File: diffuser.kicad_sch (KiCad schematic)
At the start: 4 parts, among them J5 691137710002, U8 BSR802NL6327HTSA1

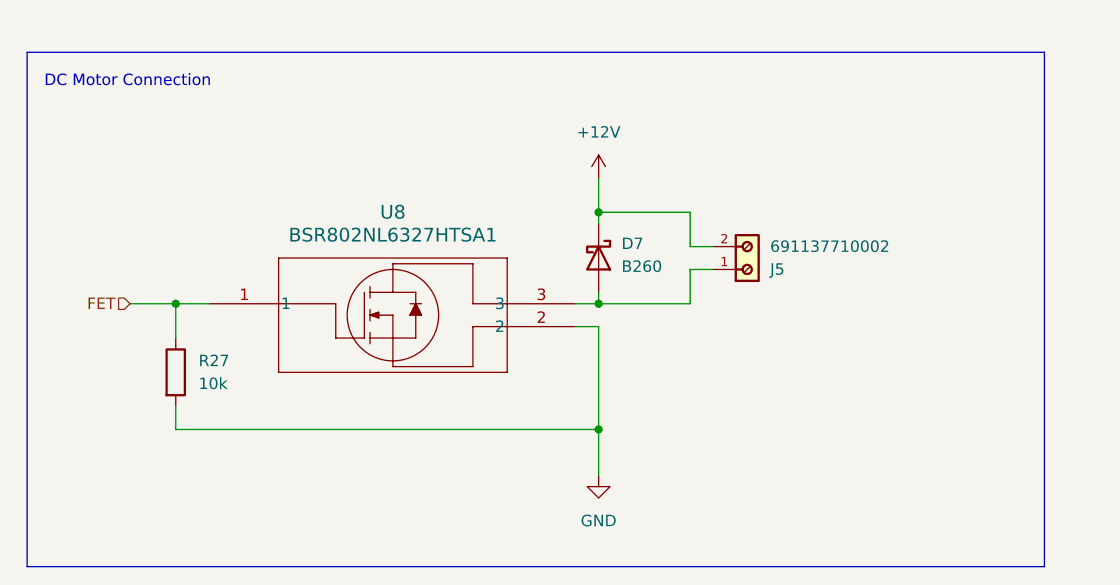
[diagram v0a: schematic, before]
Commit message: passed drc (somehow)
board routing is def cooked
verify:
- boost layout
- usb terminal layout
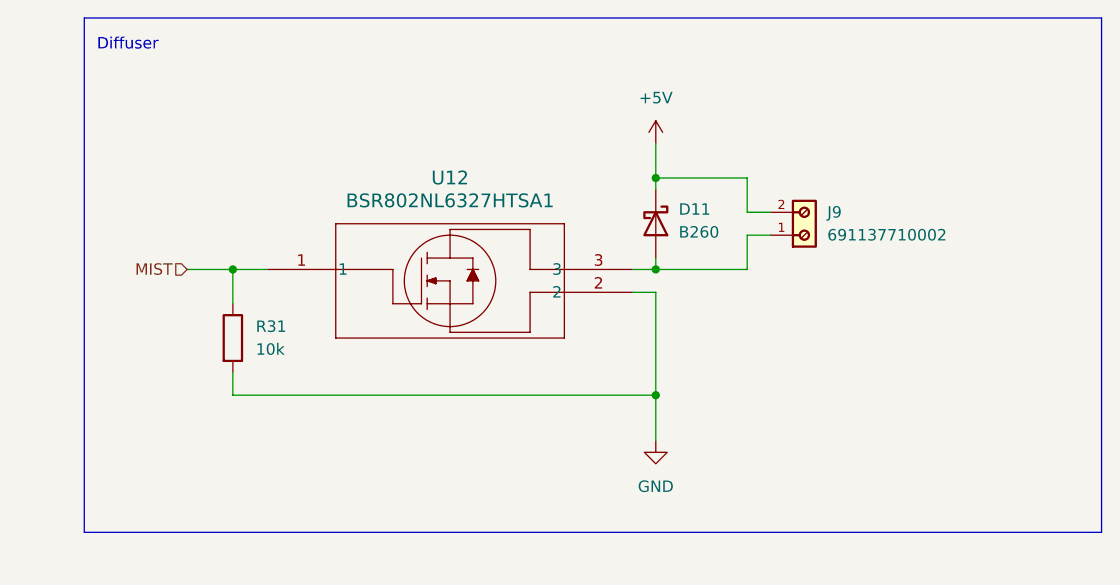
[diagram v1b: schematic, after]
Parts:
- removed D7: B260, Diode_SMD:D_SMB, symbol Diode:B260
- removed J5: 691137710002, footprints:691137710002, symbol 691137710002:691137710002
- removed R27: 10k, Resistor_SMD:R_0603_1608Metric, symbol Device:R
- removed U8: BSR802NL6327HTSA1, footprints:mosfet, symbol mosfet:BSR802NL6327HTSA1
- added D11: B260, Diode_SMD:D_SMB, symbol Diode:B260
- added J9: 691137710002, footprints:691137710002, symbol 691137710002:691137710002
- added R31: 10k, Resistor_SMD:R_0603_1608Metric, symbol Device:R
- added U12: BSR802NL6327HTSA1, footprints:mosfet, symbol mosfet:BSR802NL6327HTSA1
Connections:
- net GND: now also R31.2, U12.2
- new net: D11.2 (A), J9.1, U12.3
- new net +5V: D11.1 (K), J9.2
- new net MIST: R31.1, U12.1
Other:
- note added: "Diffuser"
- note removed: "DC Motor Connection"
